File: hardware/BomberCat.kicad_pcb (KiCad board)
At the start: 2 copper layers, 65 x 38 mm, 108 parts, among them J1 Battery, J3 MAGSPOOF, P1 USB_C_Plug_USB2.0, Q1 DMG3415U-7, SW1 RESET, SW2 GPIO, SW3 ON, SW4 SOURCE MAG, U1 PN7150B0HN_C11002E-PN7150B0HN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, U2 RP2040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

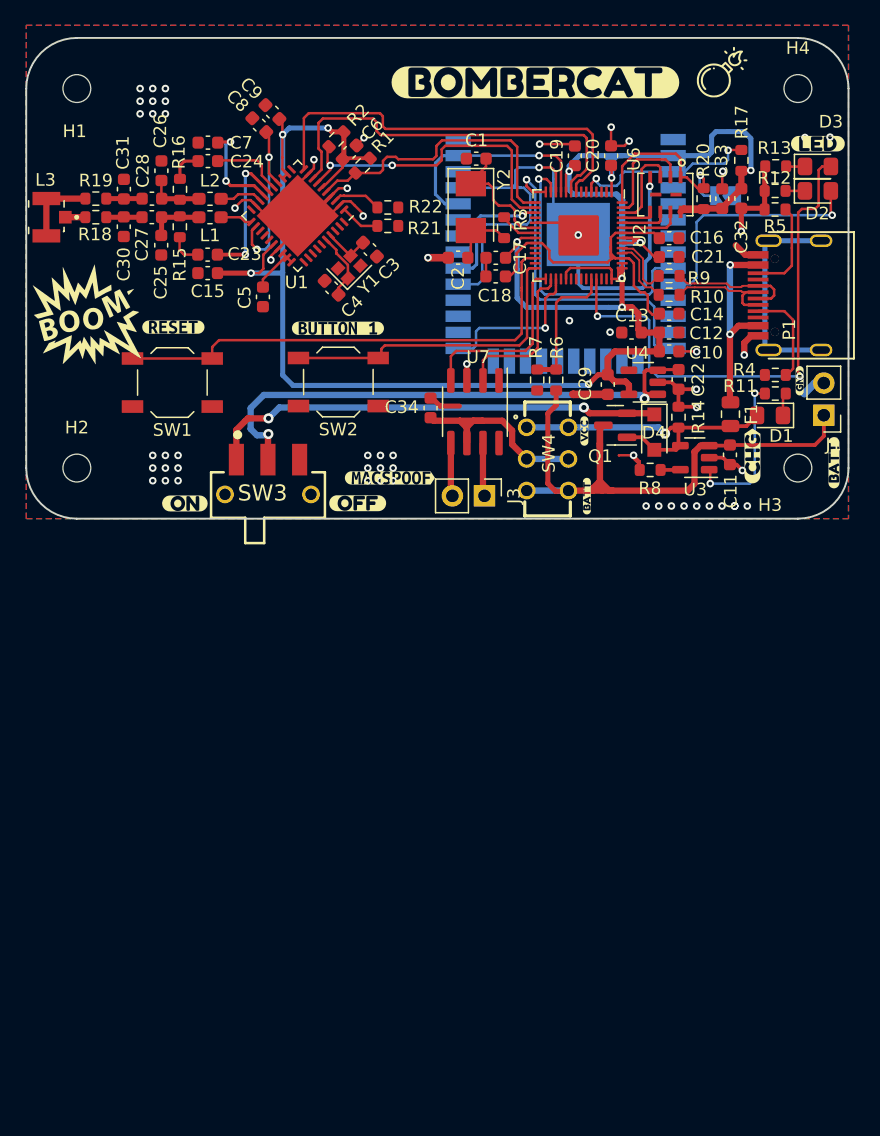
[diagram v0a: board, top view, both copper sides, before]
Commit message: feat(hw): update components labels
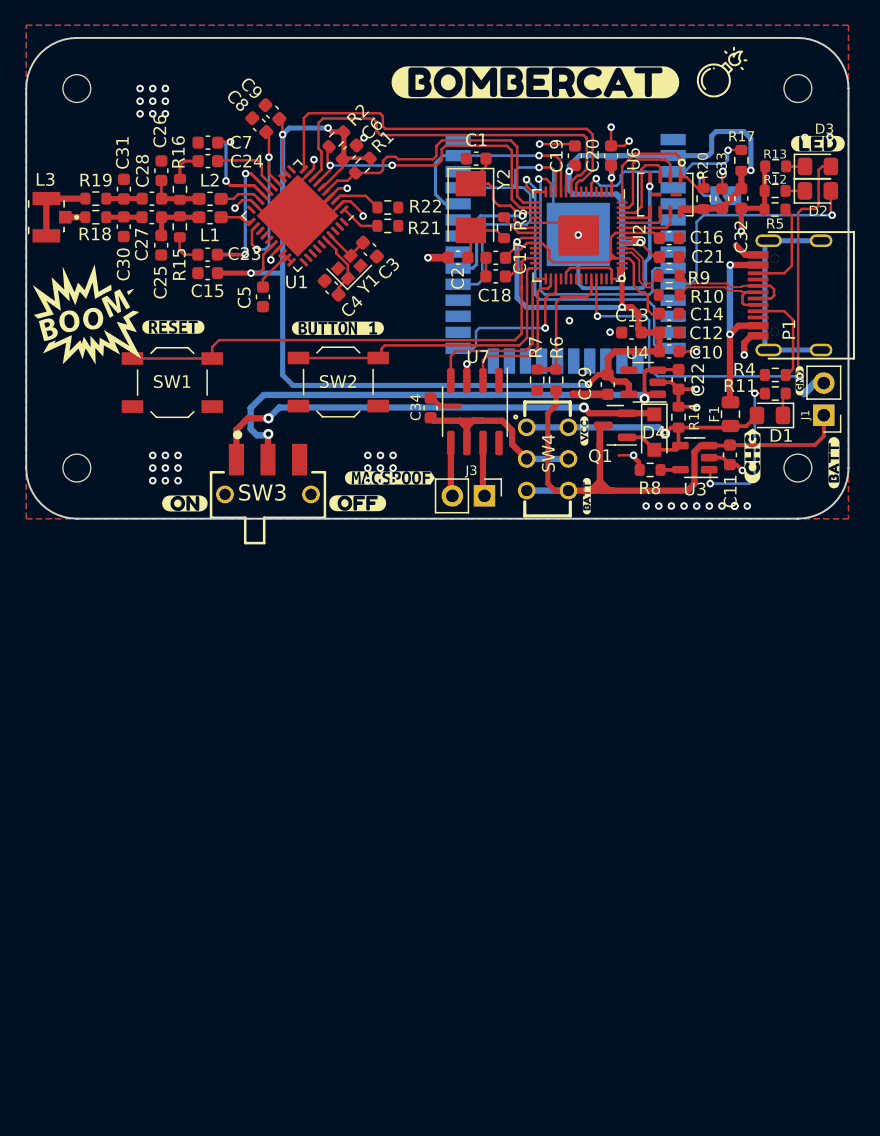
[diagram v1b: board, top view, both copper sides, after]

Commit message: feat(hw): add Embedded Antenna
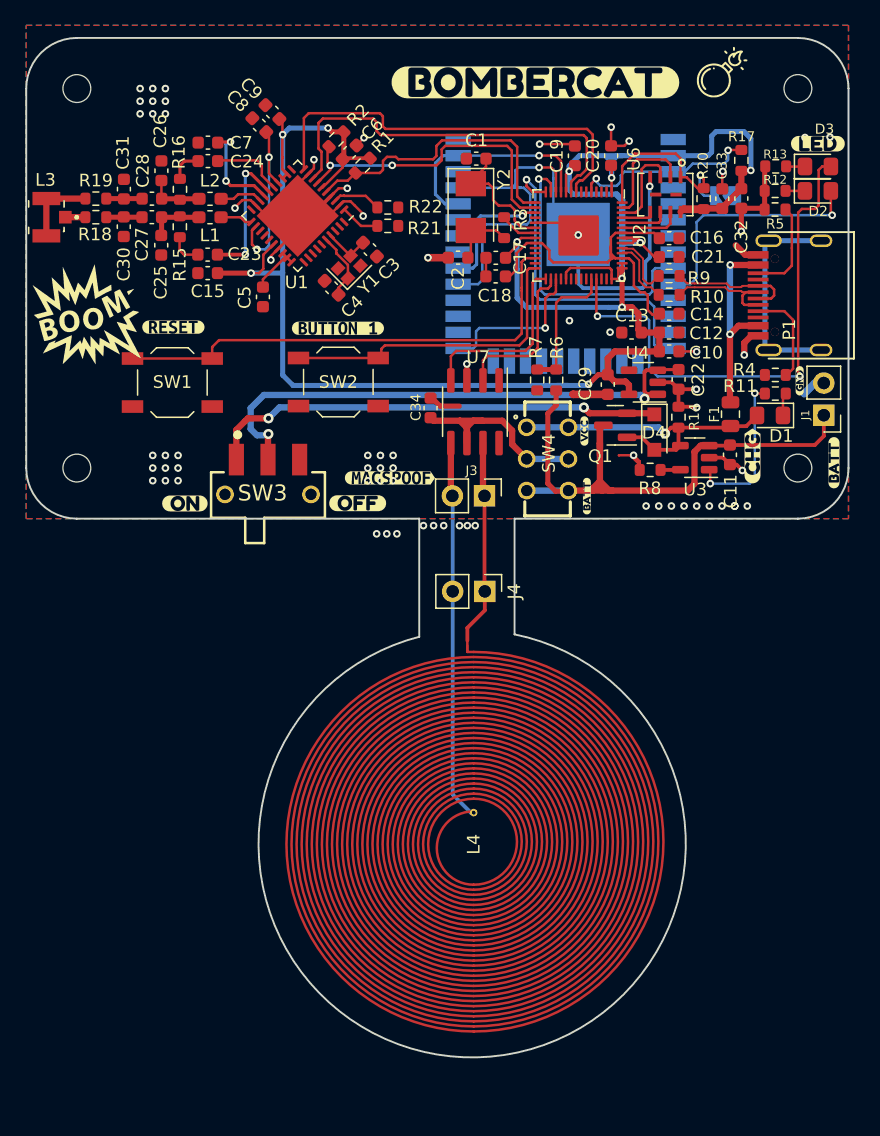
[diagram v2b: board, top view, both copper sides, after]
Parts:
- added J4: MAGSPOOF, Connector_PinHeader_2.54mm:PinHeader_1x02_P2.54mm_Vertical, F.Cu at (128.2, 179.8)
- added L4: 30t_30mm, BomberCat:Coil_30t_30mm_0.2_0.2_0.6_0.3, F.Cu at (127.4, 199.7)
- R8: value 2K -> 5.1K
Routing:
- net /OUTB: track 4.22 -> 30.1 mm
- net /OUTA: track 4.22 -> 16.2 mm
- net (no net): vias 0 -> 9
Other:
- board size 65 x 38 mm -> 65 x 80.6 mm

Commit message: feat(hw): update Antenna
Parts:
- added kibuzzard-67E317B3: G***, kibuzzard-67E317B3, F.Cu at (127.1, 170.2)
- moved J4 5.30 mm to (128.2, 185.1)
- moved L4 4.15 mm to (127.3, 203.9)
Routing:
- net /OUTA: track 16.2 -> 20.8 mm
- net /OUTB: track 30.1 -> 34.5 mm
- net (no net): vias 9 -> 18
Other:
- board size 65 x 80.6 mm -> 65 x 84.7 mm

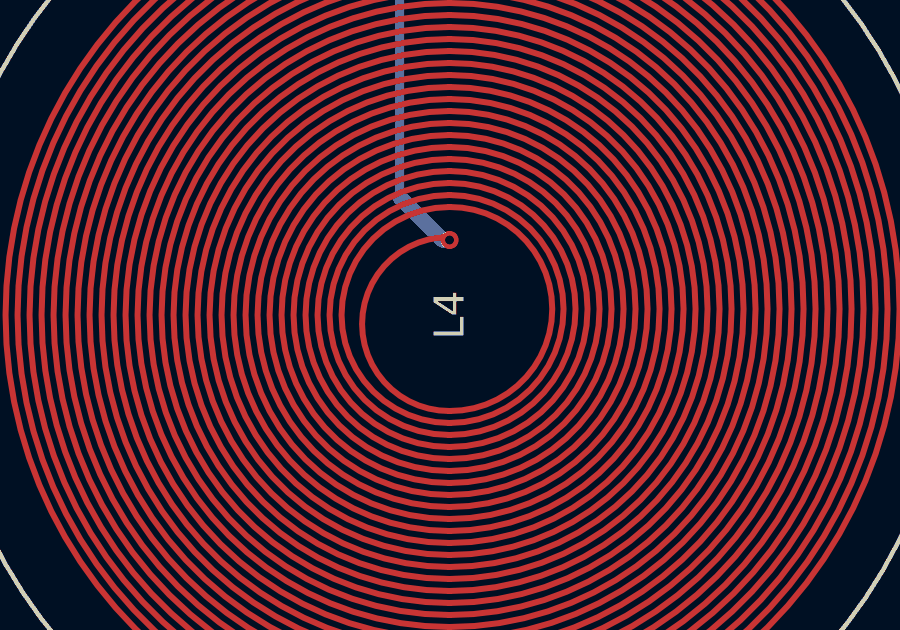
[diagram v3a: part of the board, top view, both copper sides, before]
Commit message: fix(hw): update Thickness specifications
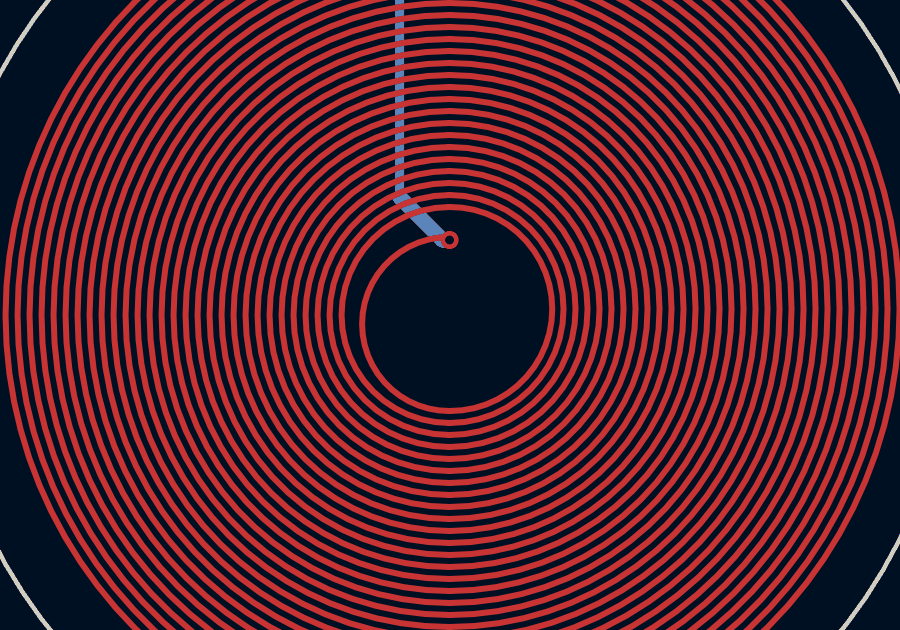
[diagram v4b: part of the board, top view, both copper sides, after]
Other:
- board text added: "Thickness: 0.8 mm"
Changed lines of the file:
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@@
 				(font
 					(size 0.001 0.001)
+					(thickness 0.15)
 				)
 			)
@@
 				(font
 					(size 0.001 0.001)
+					(thickness 0.15)
 				)
 			)
@@
 			(unlocked yes)
 			(layer "F.SilkS")
+			(hide yes)
 			(effects
 				(font
@@
 		(layer "Edge.Cuts")
 	)
+	(gr_text "Thickness: 0.8 mm"
+		(at 162.45 157.15 0)
+		(layer "Cmts.User")
+		(effects
+			(font
+				(size 2 2)
+				(thickness 0.3)
+			)
+			(justify left bottom)
+		)
+	)
 	(dimension

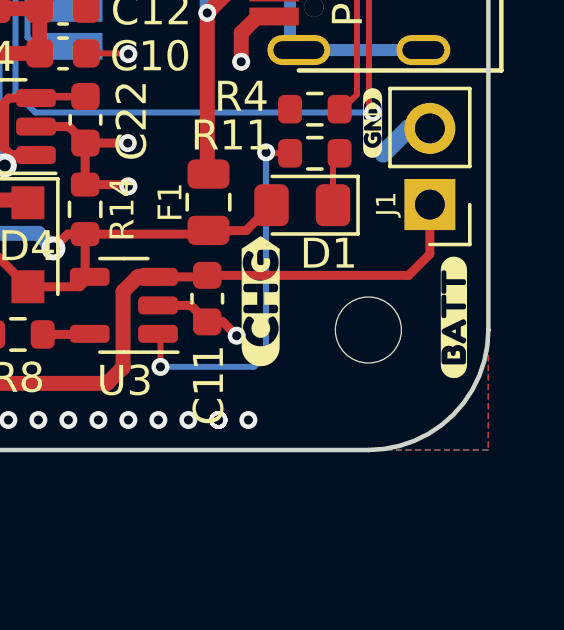
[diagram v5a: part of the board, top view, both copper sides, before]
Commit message: fix(hw): Update Batt Label
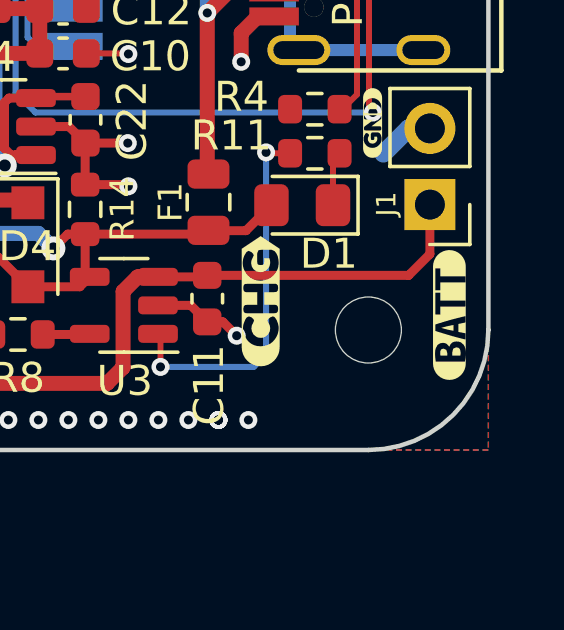
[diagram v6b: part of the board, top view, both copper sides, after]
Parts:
- removed kibuzzard-62EEB113: G***, kibuzzard-62EEB113
- added kibuzzard-67F445A5: G***, kibuzzard-67F445A5, F.Cu at (155.7, 169.5)

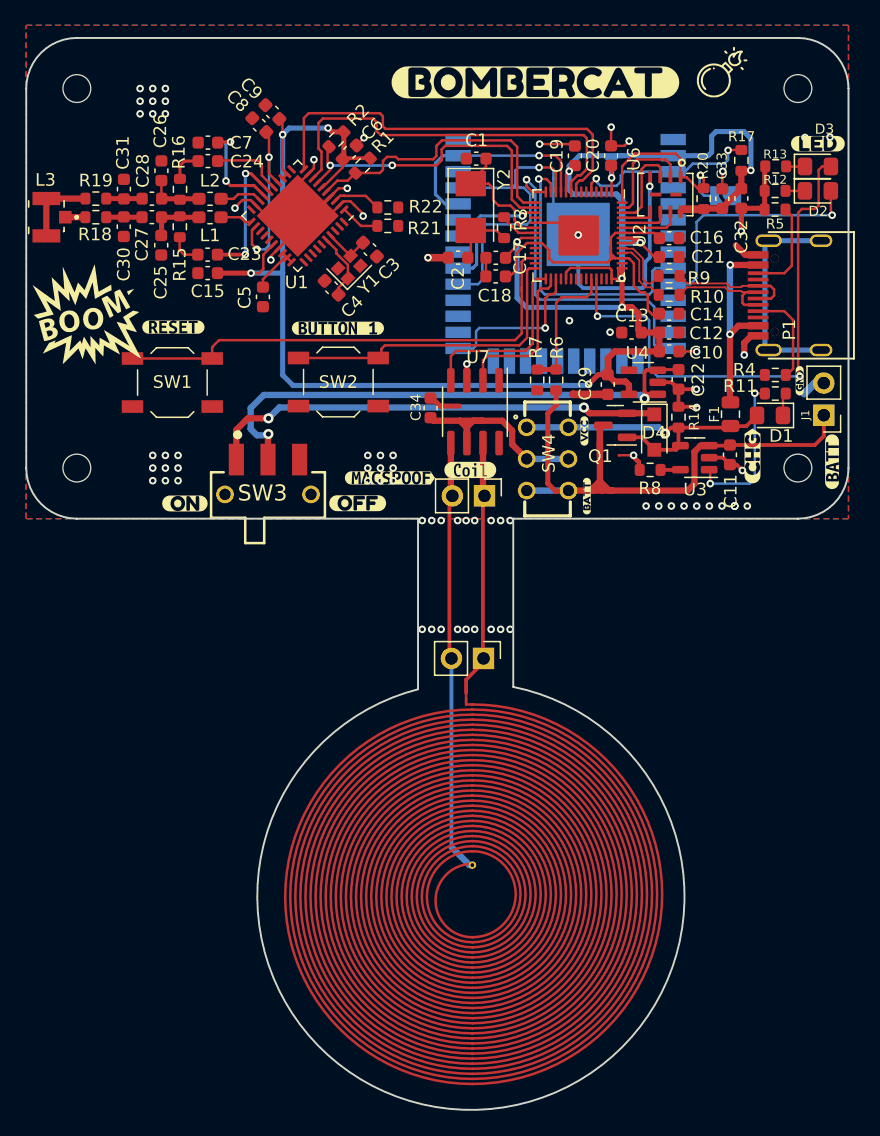
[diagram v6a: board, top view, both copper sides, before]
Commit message: fix(hw): update routes and labels
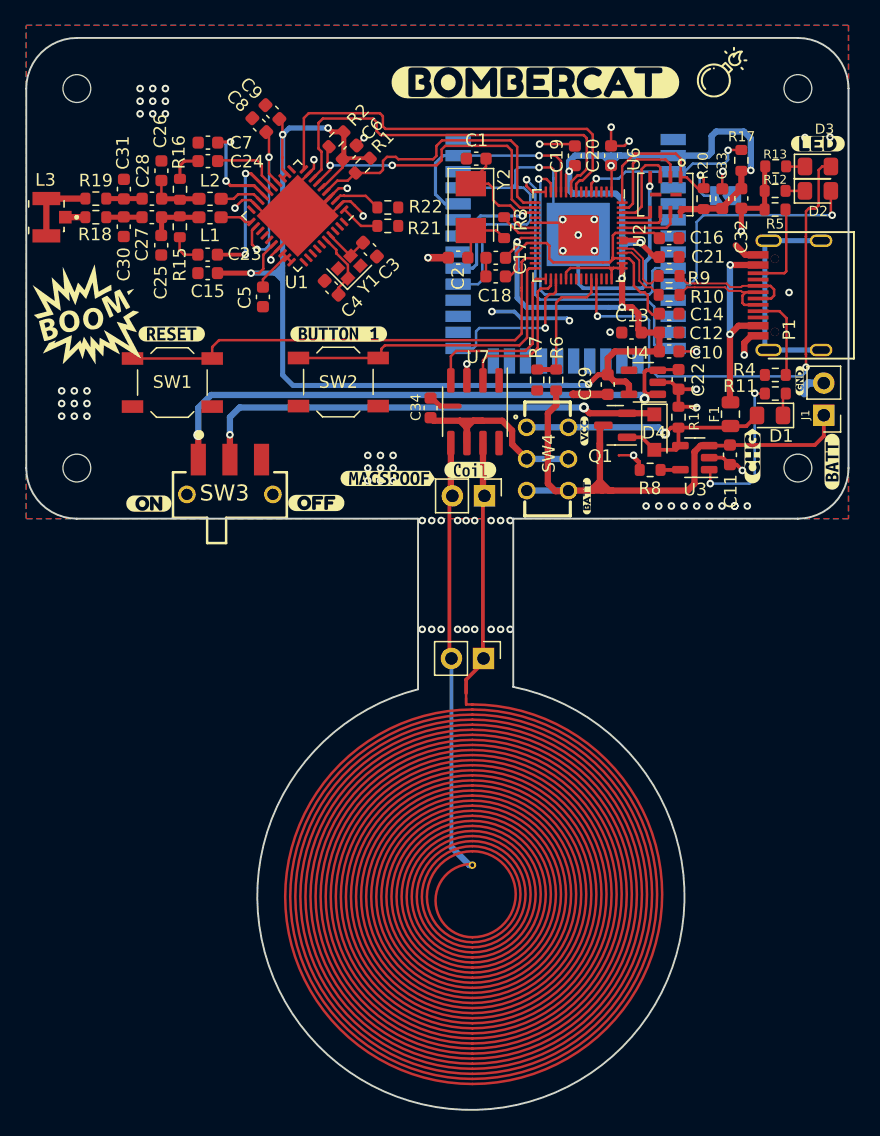
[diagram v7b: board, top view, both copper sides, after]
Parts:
- removed kibuzzard-62CC5774: G***, kibuzzard-62CC5774
- removed kibuzzard-62CC5787: G***, kibuzzard-62CC5787
- removed kibuzzard-62CC57AB: G***, kibuzzard-62CC57AB
- removed kibuzzard-62E1B24A: G***, kibuzzard-62E1B24A
- removed kibuzzard-62E1B2BF: G***, kibuzzard-62E1B2BF
- removed kibuzzard-67F445A5: G***, kibuzzard-67F445A5
- added kibuzzard-67F6D96D: G***, kibuzzard-67F6D96D, F.Cu at (103.5, 159.4)
- added kibuzzard-67F6D992: G***, kibuzzard-67F6D992, F.Cu at (116.7, 159.4)
- added kibuzzard-67F6D9A7: G***, kibuzzard-67F6D9A7, F.Cu at (155.7, 169.5)
- added kibuzzard-67F6E51F: G***, kibuzzard-67F6E51F, F.Cu at (120.6, 170.8)
- added kibuzzard-67F6E5D9: G***, kibuzzard-67F6E5D9, F.Cu at (101.7, 172.8)
- added kibuzzard-67F6E601: G***, kibuzzard-67F6E601, F.Cu at (114.9, 172.8)
- R8: value 5.1K -> 5k1
- U3: value MCP73831-3-OT -> MCP73831T-2DCI/OT
- moved SW3 3.01 mm to (108.1, 170.3)
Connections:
- C22 pad 1: Net-(SW3-B) -> Net-(SW3-A)
- L4 pad : /OUTB -> (no net)
- SW3 pad 1: Net-(D4-K) -> Net-(SW3-A)
- SW3 pad 2: Net-(SW3-B) -> Net-(D4-K)
- U4 pad 1: Net-(SW3-B) -> Net-(SW3-A)
- U4 pad 3: Net-(SW3-B) -> Net-(SW3-A)
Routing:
- net Net-(SW3-A): track 0.00 -> 46.6 mm, vias 0 -> 2
- net Net-(SW3-B): track 43.7 -> 0.00 mm, vias 2 -> 0
- net +3V3: track 177.7 -> 168.7 mm
- net GND: track 116.9 -> 123.6 mm, vias 63 -> 69
- net Net-(D4-K): track 36.4 -> 37.4 mm
- net /ESP_RESET: track 15.0 -> 14.1 mm
- net Net-(P1-CC): track 7.69 -> 7.06 mm

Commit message: feat(hw): update routes and resize coil arm
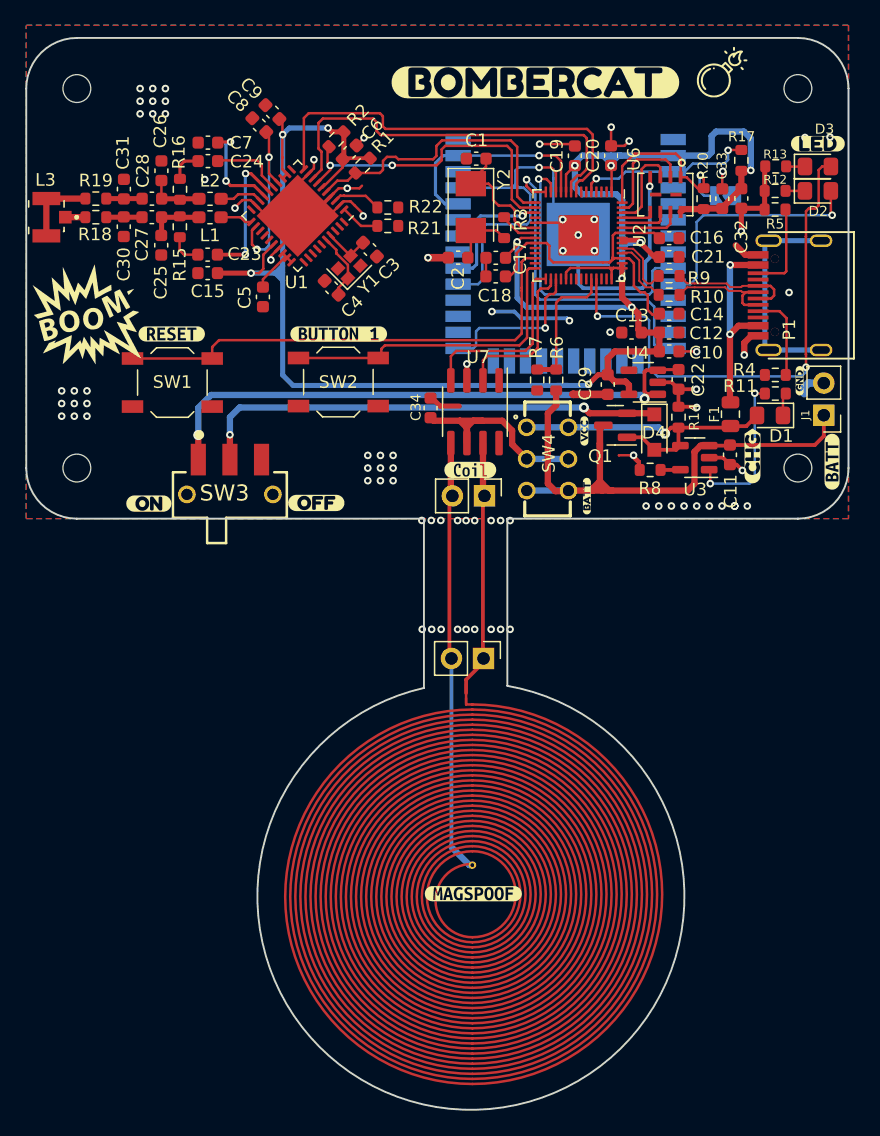
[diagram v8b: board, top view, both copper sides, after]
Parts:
- removed kibuzzard-67F6E51F: G***, kibuzzard-67F6E51F
- added kibuzzard-67FD52FB: G***, kibuzzard-67FD52FB, F.Cu at (127.3, 203.6)
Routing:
- net GND: track 123.6 -> 124.8 mm, vias 69 -> 70
- net +3V3: track 168.7 -> 167.9 mm
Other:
- outline, holes or cut-outs redrawn
